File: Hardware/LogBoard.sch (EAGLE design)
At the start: 53 parts, among them CN1 uSD Card, IC1 ESP12E, IC2 DS1391, IC3 FT232RQ, IC4 MAX14591, IC5 MAX14591, IC6 MAX1811, IC7 MAX8625, IC8 DS1722, X1 32.768k

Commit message: Updated Eagle PCB
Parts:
- C1, C10, C11, C13, C14, C2, C3, C4, C5, C6, C7, C8, C9: device 000_Renan_Duarte:1-CAP-SMD-0603 -> 000_Renan_Duarte:1-CAPACITORSMD-0603
- C12: device 000_Renan_Duarte:1-CAP-POL -> 000_Renan_Duarte:1-CAPACITOR-POL
- L3: device 000_Renan_Duarte:7-IND-3X3 -> 000_Renan_Duarte:2-INDUCTOR3X3
- R1, R10, R11, R12, R13, R2, R3, R4, R5, R6, R7, R8, R9: device 000_Renan_Duarte:0-RES-SMD-0603 -> 000_Renan_Duarte:0-RESISTORSMD-0603
- SV2: device con-lstb:MA09-2 -> 000_Renan_Duarte:PIN-HEADER-9X2
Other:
- note added: "MISTAKES OF v1: - USD CD was not connected - RTC RST (DS1391) causes ESP not to boot. Disconnect this signal or use DS1390"
- note removed: "MISTAKES OF v1: - USD CD was not connected - RTC RST (DS1391) causes ESP to crash on boot. Disconnect this signal or use DS1390"
- moved on the sheet: BAT+, BAT-, C10, C11, C12, C5, C6, C9, CN1, IC2, IC6, IC7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

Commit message: Updated BOM
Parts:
- C11, C4: value 10u/10V -> 1u/10V
- C12: value 0.33F/5.5V -> 100n/10V; device 000_Renan_Duarte:1-CAPACITOR-POL -> 000_Renan_Duarte:1-CAPACITORSMD-0603
- C13, C14: value 1u/10V -> 100n/10V
- C15: value 47u/6.3V -> 10u/10V; device rcl:CPOL-EUCT3528 -> 000_Renan_Duarte:1-CAPACITORSMD-0603
- C16: value 47u6.3V -> 100n/10V; device rcl:CPOL-EUCT3528 -> 000_Renan_Duarte:1-CAPACITORSMD-0603
- C2, C3: value 100n/10V -> 47u/6.3V; device 000_Renan_Duarte:1-CAPACITORSMD-0603 -> 000_Renan_Duarte:1-CAPACITOR-POLCT3528
- C5: value 100n/10V -> 1u/10V
- C6: value 1u/10V -> 0.33F/5.5V; device 000_Renan_Duarte:1-CAPACITORSMD-0603 -> 000_Renan_Duarte:1-CAPACITOR-POL5X11.5
- C7: value 100n/10V -> 10u/10V
- IC2: value DS1391 -> FT232RQ; device 000_Renan_Duarte:IC-DS1394 -> 000_Renan_Duarte:IC-FT232RQ
- IC3: value FT232RQ -> MAX14591ETA+; device 000_Renan_Duarte:IC-FT232RQ -> 000_Renan_Duarte:IC-MAX14591
- IC4: value MAX14591 -> MAX14591ETA+
- IC5: value MAX14591 -> MAX1811ESA+; device 000_Renan_Duarte:IC-MAX14591 -> 000_Renan_Duarte:IC-MAX1811
- IC6: value MAX1811 -> MAX8625AETD+; device 000_Renan_Duarte:IC-MAX1811 -> 000_Renan_Duarte:IC-MAX8625
- IC7: value MAX8625 -> DS1391U-33+; device 000_Renan_Duarte:IC-MAX8625 -> 000_Renan_Duarte:IC-DS1394
- IC8: value DS1722 -> DS1722S+
- J1: value (none) -> C77238
- J2: value uSD Card -> THD2528-11SD-GF
- J3: value (none) -> HEADER 2x9 180
- Q1: value (none) -> BC847BS-7-F
- R1: value 0/WAKE -> 10k
- R10: value 1k -> 33
- R11: value 390k -> 33
- R12: value 100k -> 1k
- R13: value 10k -> 1k
- R2: value 10k -> 0/WAKE
- R3: value 10k -> 390k
- R4: value 10k -> 100k
- R7, R9: value 33 -> 10k
- R8: value 1k -> 10k
- S1: value POWER -> SK-3296S-01-L1
- S2: value RST -> TS24CA
- renumbered BAT+ to PAD1, BAT- to PAD2, CN1 to J2, L3 to L1, SV2 to J3
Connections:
- net 3V3: now also C13.2, C15.1, C16.1, C2.P, C3.P, C4.1, C5.1, IC3.VCC, IC6.OUT, IC7.VCC, R1.2, R5.2, R7.2; no longer C10.1, C11.1, C13.1, C14.1, C15.+, C16.+, C8.2, IC2.VCC, IC5.VCC, IC7.OUT, R2.2, R3.2, R4.2
- net 3V3FTDI: now also C12.2, C8.2, IC2.!RESET, IC2.3V3OUT, IC2.VCCIO, IC3.!TL, IC3.VL; no longer C3.2, C7.2, IC3.!RESET, IC3.3V3OUT, IC3.VCCIO, IC5.!TL, IC5.VL
- net 5V0: now also C7.2, C9.2, IC2.VCC, IC5.EN, IC5.IN, IC5.SELI, R12.1, R13.2; no longer C2.2, C4.2, IC3.VCC, IC6.EN, IC6.IN, IC6.SELI, R10.2, R8.1
- net DTR: now also IC4.IOVCC2, R9.2; no longer IC5.IOVCC2, R6.2
- net FTDI_DTR: now also IC2.!DTR, IC4.IOVL2; no longer IC3.!DTR, IC5.IOVL2
- net FTDI_RTS: now also IC2.!RTS, IC3.IOVL1; no longer IC3.!RTS, IC4.IOVL1
- net FTDI_RX: now also IC2.RXD, IC3.IOVL2; no longer IC3.RXD, IC4.IOVL2
- net FTDI_TX: now also IC2.TXD, IC4.IOVL1; no longer IC3.TXD, IC5.IOVL1
- net GND: now also C12.1, C13.1, C15.2, C16.2, C2.N, C3.N, C4.2, C6.N, C9.1, IC2.GND@1, IC2.GND@2, IC2.GND@A, IC2.TEST, IC5.GND@1, IC6.!SKIP, IC6.FB, R4.1, R6.1; no longer C12.N, C13.2, C15.-, C16.-, C2.1, C3.1, C4.1, C6.2, C9.2, IC3.GND@1, IC3.GND@2, IC3.GND@A, IC3.TEST, IC6.GND@1, IC7.!SKIP, IC7.FB, R12.1, R13.1
- net GPIO0: now also R5.1; no longer R3.1
- net GPIO1/TX: now also IC3.IOVCC2; no longer IC4.IOVCC2
- net GPIO10/CSRTC: now also IC7.CS; no longer IC2.CS
- net GPIO12/MISO: now also IC7.MISO; no longer IC2.MISO
- net GPIO13/MOSI: now also IC7.MOSI; no longer IC2.MOSI
- net GPIO14/CLK: now also IC7.CLK; no longer IC2.CLK
- net GPIO15: now also R6.2; no longer R13.2
- net GPIO16: now also R2.1; no longer R1.1
- net GPIO2/INTRTC: now also IC7.INT, R7.1; no longer IC2.INT, R4.1
- net GPIO3/RX: now also IC4.IOVCC1; no longer IC5.IOVCC1
- net LED_CHG: now also IC5.!CHG; no longer IC6.!CHG
- net LED_RX: now also IC2.CBUS1, R11.1; no longer IC3.CBUS1, R9.1
- net LED_TX: now also IC2.CBUS0, R10.1; no longer IC3.CBUS0, R7.1
- net N$1: now also R8.1; no longer R5.1
- net N$10: now also IC5.SELV; no longer IC6.SELV
- net N$11: now also IC6.LX1; no longer IC7.LX1
- net N$16: now also IC6.LX2; no longer IC7.LX2
- net N$17: now also R3.1, R4.2; no longer R11.1, R12.2
- net N$18: now also IC7.X1; no longer IC2.X1
- net N$19: now also IC7.X2; no longer IC2.X2
- net N$2: now also R9.1; no longer R6.1
- net N$20: now also C14.1, IC6.REF; no longer C9.1, IC7.REF
- net N$22: now also R13.1; no longer R10.1
- net N$4: now also IC2.USBDM; no longer IC3.USBDM
- net N$5: now also IC2.USBDP; no longer IC3.USBDP
- net N$6: now also R10.2; no longer R7.2
- net N$7: now also R11.2; no longer R9.2
- net N$8: now also R12.2; no longer R8.2
- net PWRON: now also IC6.ON; no longer IC7.ON
- net RST: now also R1.1, R2.2; no longer R1.2, R2.1
- net RTS: now also IC3.IOVCC1, R8.2; no longer IC4.IOVCC1, R5.2
- net VBAT: now also C10.1, C11.1, IC5.BATT, IC6.IN, R3.2; no longer C5.1, C6.1, IC6.BATT, IC7.IN, R11.2
- net VBKP: now also C6.P, IC7.VBKP; no longer C12.P, IC2.VBKP
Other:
- note added: "MISTAKES OF v1: - USD CD was not connected - RTC RST (DS1391) causes ESP not to boot. Disconnect this signal or use DS1390 - S2 footprint is wrong"
- note removed: "MISTAKES OF v1: - USD CD was not connected - RTC RST (DS1391) causes ESP not to boot. Disconnect this signal or use DS1390"
- moved on the sheet: C10, C11, C13, C14, C4, C5, C7, C8, C9, IC4, IC5, R1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

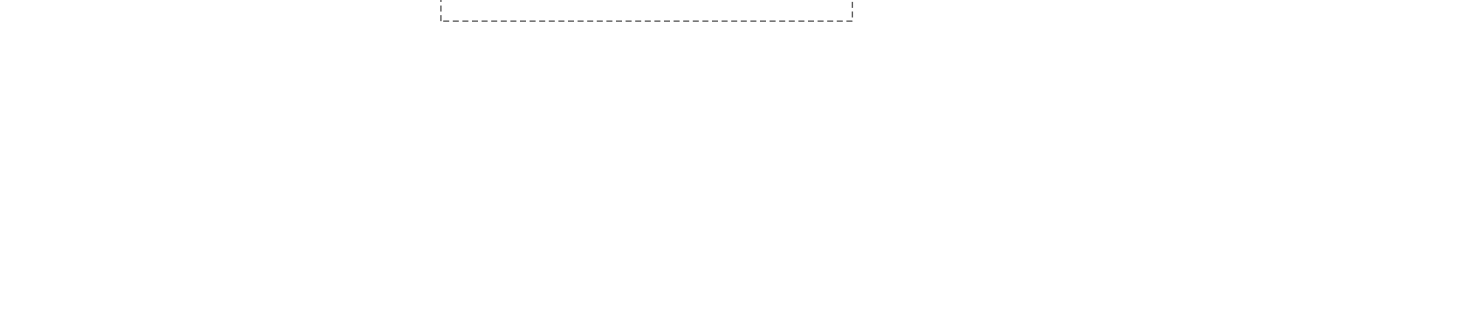
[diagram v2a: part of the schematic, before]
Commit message: Added info regarding SPI DIO mode
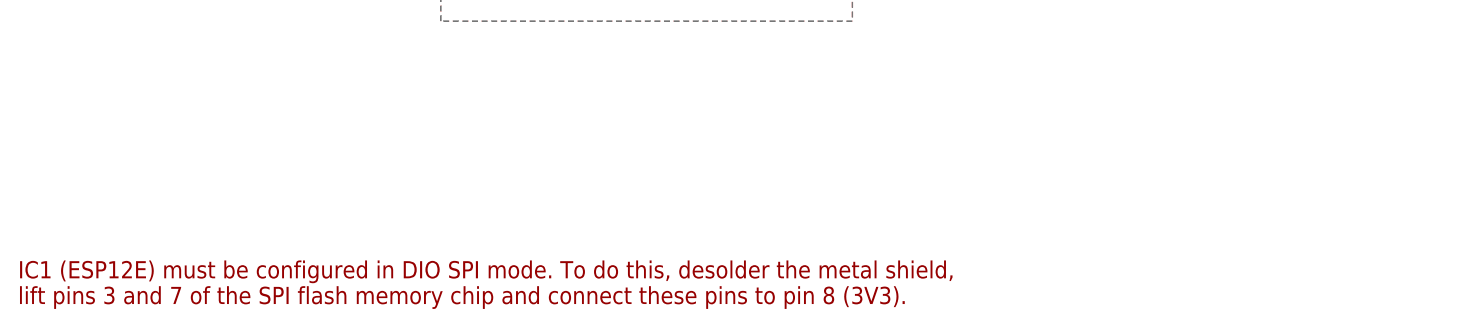
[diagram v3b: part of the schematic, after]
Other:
- note added: "IC1 (ESP12E) must be configured in DIO SPI mode. To do this, desolder the metal shield, lift pins 3 and 7 of the SPI flash memory chip and connect these pins to pin 8 (3V3)."
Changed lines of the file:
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@@
 <text x="77.47" y="-274.32" size="2.54" layer="94" font="vector" align="top-left">v1</text>
 <text x="6.35" y="-269.24" size="2.54" layer="94" font="vector" align="top-left">Renan R. Duarte</text>
+<text x="-290.83" y="-275.59" size="1.905" layer="94" font="vector" ratio="15" align="top-left">IC1 (ESP12E) must be configured in DIO SPI mode. To do this, desolder the metal shield,
+lift pins 3 and 7 of the SPI flash memory chip and connect these pins to pin 8 (3V3).</text>
 </plain>
 <instances>
